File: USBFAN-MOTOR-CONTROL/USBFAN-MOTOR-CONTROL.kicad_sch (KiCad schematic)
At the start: 27 parts

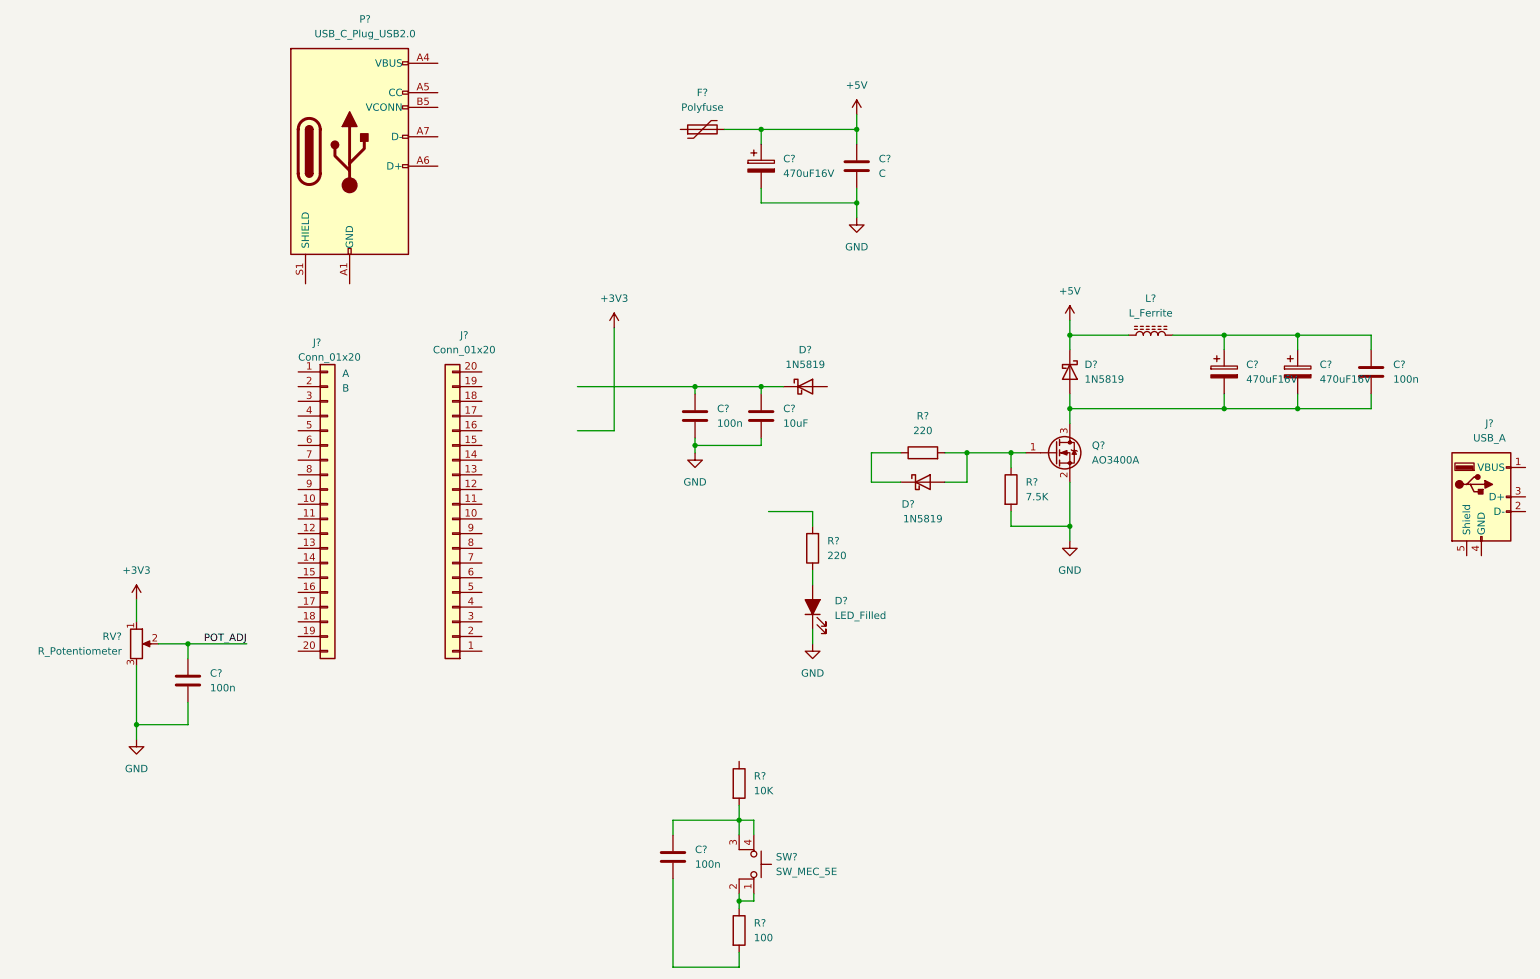
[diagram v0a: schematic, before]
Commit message: schematics finalized and pcb generated.
 Changes to be committed:
	modified:   USBFAN-MOTOR-CONTROL/USBFAN-MOTOR-CONTROL.kicad_pcb
	modified:   USBFAN-MOTOR-CONTROL/USBFAN-MOTOR-CONTROL.kicad_prl
	modified:   USBFAN-MOTOR-CONTROL/USBFAN-MOTOR-CONTROL.kicad_sch
	new file:   USBFAN-MOTOR-CONTROL/fp-info-cache
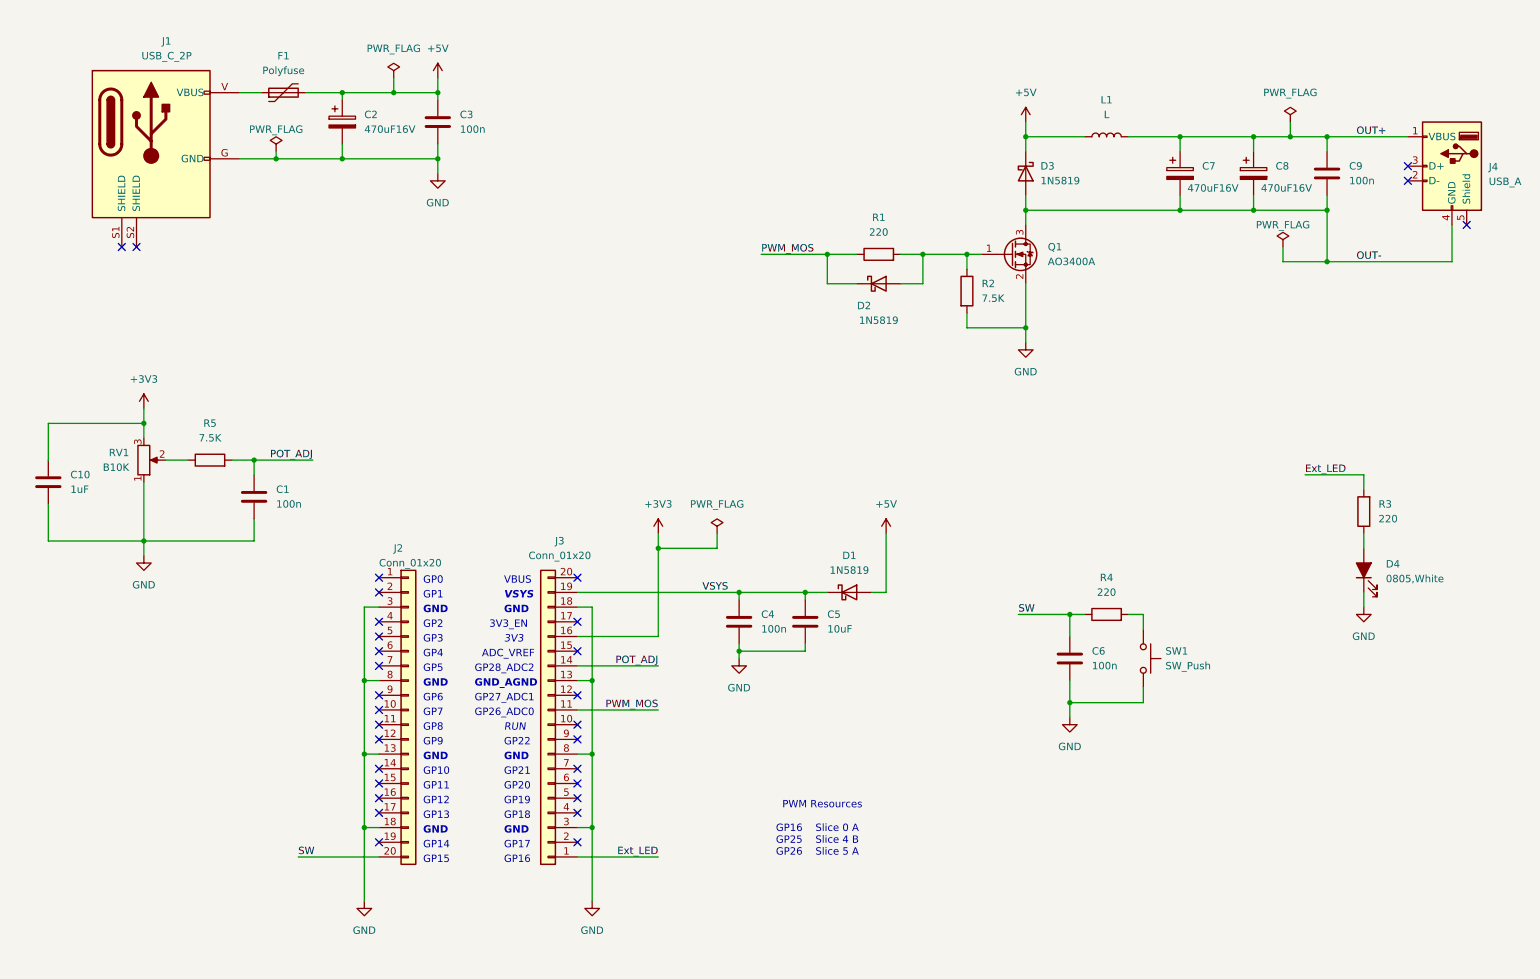
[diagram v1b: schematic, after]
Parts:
- removed J?: USB_A, symbol Connector:USB_A
- removed L?: L_Ferrite, symbol Device:L_Ferrite
- removed P?: USB_C_Plug_USB2.0, symbol Connector:USB_C_Plug_USB2.0
- removed R?: 100, symbol Device:R
- removed R?: 10K, symbol Device:R
- removed SW?: SW_MEC_5E, symbol Switch:SW_MEC_5E
- added C10: 1uF, Capacitor_SMD:C_0805_2012Metric_Pad1.18x1.45mm_HandSolder, symbol Device:C
- added J1: USB_C_2P, pcblib_new599 Library:USB_TYPE_C_2P_THT_90, symbol symbol_lib_new599_Library:USB_C_2P
- added J4: USB_A, Connector_USB:USB_A_CONNFLY_DS1095-WNR0, symbol Connector:USB_A
- added L1: L, Inductor_THT:L_Radial_D10.0mm_P5.00mm_Fastron_07M, symbol Device:L
- added R4: 220, Resistor_SMD:R_0603_1608Metric_Pad0.98x0.95mm_HandSolder, symbol Device:R
- added R5: 7.5K, Resistor_SMD:R_0603_1608Metric_Pad0.98x0.95mm_HandSolder, symbol Device:R
- added SW1: SW_Push, Button_Switch_THT:SW_PUSH_6mm_H7.3mm, symbol Switch:SW_Push
- C1, C4, C6, C9: renamed from C?; footprint (none) -> Capacitor_SMD:C_0603_1608Metric_Pad1.08x0.95mm_HandSolder
- C2, C7, C8: renamed from C?; footprint (none) -> Capacitor_THT:CP_Radial_D8.0mm_P3.50mm
- C3: renamed from C?; value C -> 100n; footprint (none) -> Capacitor_SMD:C_0603_1608Metric_Pad1.08x0.95mm_HandSolder
- C5: renamed from C?; footprint (none) -> Capacitor_SMD:C_0805_2012Metric_Pad1.18x1.45mm_HandSolder
- D1, D2, D3: renamed from D?; footprint Diode_THT:D_DO-41_SOD81_P10.16mm_Horizontal -> Diode_SMD:D_SOD-323_HandSoldering
- D4: renamed from D?; value LED_Filled -> 0805,White; footprint (none) -> LED_SMD:LED_0805_2012Metric_Pad1.15x1.40mm_HandSolder
- F1: renamed from F?; footprint (none) -> Fuse:Fuse_0805_2012Metric_Pad1.15x1.40mm_HandSolder
- J2, J3: renamed from J?; footprint (none) -> Connector_PinSocket_2.54mm:PinSocket_1x20_P2.54mm_Vertical
- R1, R2, R3: renamed from R?; footprint (none) -> Resistor_SMD:R_0603_1608Metric_Pad0.98x0.95mm_HandSolder
- RV1: renamed from RV?; value R_Potentiometer -> B10K; footprint (none) -> pcblib_new599 Library:POT_SINGLE_WH148
- gave numbers to parts that had none: 1
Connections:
- net +3V3: now also J3.16 (Pin_16), RV1.3, C10.1; no longer RV1.1
- net +5V: now also D1.2 (A), L1.1
- net GND: now also C6.2, J2.13 (Pin_13), J2.18 (Pin_18), J2.3 (Pin_3), J2.8 (Pin_8), J3.13 (Pin_13), J3.18 (Pin_18), J3.3 (Pin_3), J3.8 (Pin_8), RV1.1, C10.2, J1.G (GND), SW1.2; no longer RV1.3
- net POT_ADJ: now also J3.14 (Pin_14), R5.2; no longer RV1.2
- net VSYS: now reaches C4.1, C5.1, D1.1 (K)
- net VSYS: now also J3.19 (Pin_19)
- net SW: now reaches C6.1
- net SW: now also J2.20 (Pin_20), R4.1
- net OUT+: now reaches C7.1, C8.1, C9.1
- net OUT+: now also J4.1 (VBUS), L1.2
- net OUT-: now reaches C7.2, C8.2, C9.2, D3.2 (A), Q1.3 (D)
- net OUT-: now also J4.4 (GND)
- net PWM_MOS: now reaches D2.1 (K), R1.1
- net PWM_MOS: now also J3.11 (Pin_11)
- net Ext_LED: now reaches R3.2
- net Ext_LED: now also J3.1 (Pin_1)
- net at F1.1: now also J1.V (VBUS)
- new net: R4.2, SW1.1
- new net: R5.1, RV1.2
- no-connect marks 0 -> 31
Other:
- note added: "3V3"
- note added: "3V3_EN"
- note added: "ADC_VREF"
- note added: "GND"
- note added: "GND_AGND"
- note added: "GP0"
- note added: "GP1"
- note added: "GP10"
- note added: "GP11"
- note added: "GP12"
- note added: "GP13"
- note added: "GP14"
- note added: "GP15"
- note added: "GP16"
- note added: "GP17"
- note added: "GP18"
- note added: "GP19"
- note added: "GP2"
- note added: "GP20"
- note added: "GP21"
- note added: "GP22"
- note added: "GP26_ADC0"
- note added: "GP27_ADC1"
- note added: "GP28_ADC2"
- note added: "GP3"
- note added: "GP4"
- note added: "GP5"
- note added: "GP6"
- note added: "GP7"
- note added: "GP8"
- note added: "GP9"
- note added: "PWM Resources GP16 Slice 0 A GP25 Slice 4 B GP26 Slice 5 A"
- note added: "RUN"
- note added: "VBUS"
- note added: "VSYS"
- note removed: "A"
- note removed: "B"
- moved on the sheet: C1, C2, C3, C4, C5, C6, C7, C8, C9, D1, D2, D3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
